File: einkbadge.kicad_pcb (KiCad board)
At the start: 2 copper layers, 108.2 x 99.1 mm, 427 parts, among them J1 USB_C_Receptacle_USB2.0_14P, J2 Conn_01x03, J3 Conn_01x14_Pin, J4 Conn_01x16_Pin, Q1 Si1308EDL, SW1 SW_Push, SW2 SW_Push, SW3 SW_Push, SW4 SW_Push, SW5 SW_Push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

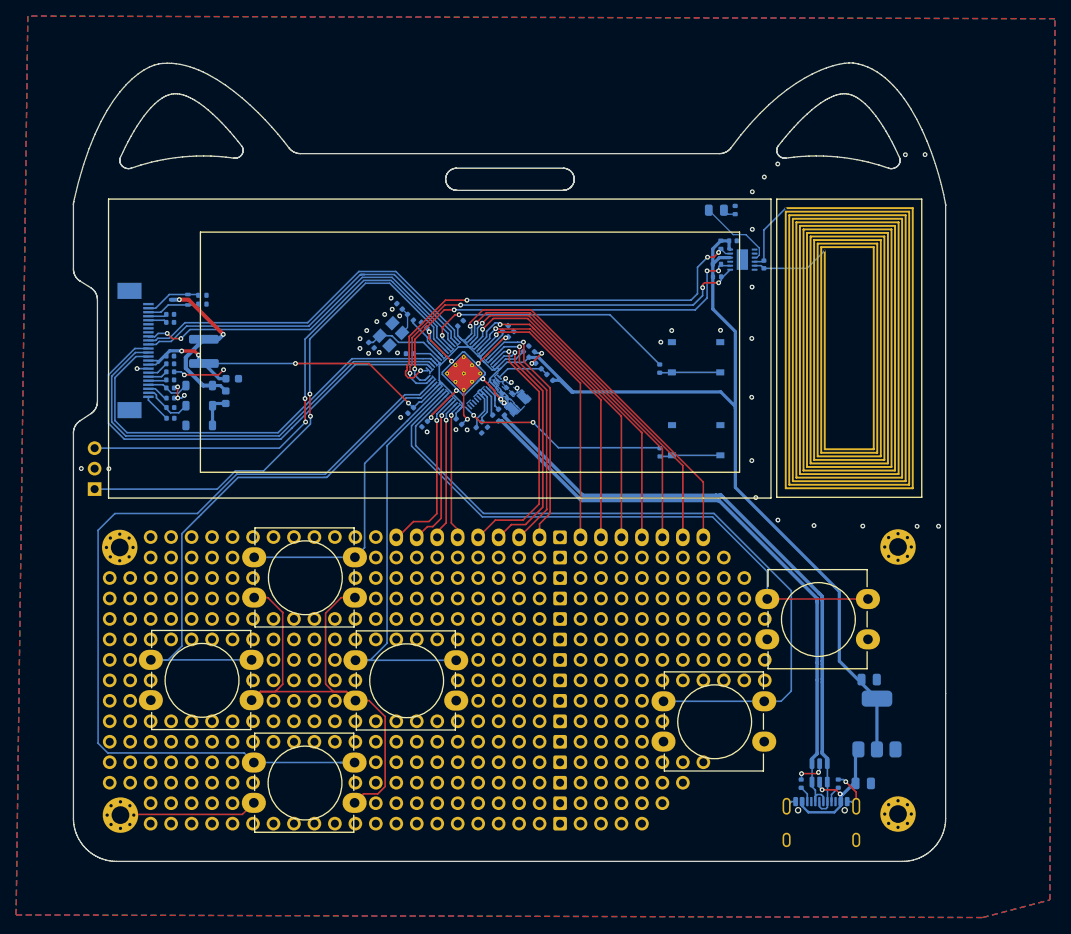
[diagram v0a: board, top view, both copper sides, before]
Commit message: add silkscreen, reroute eink connector
also removed part label silkscreen
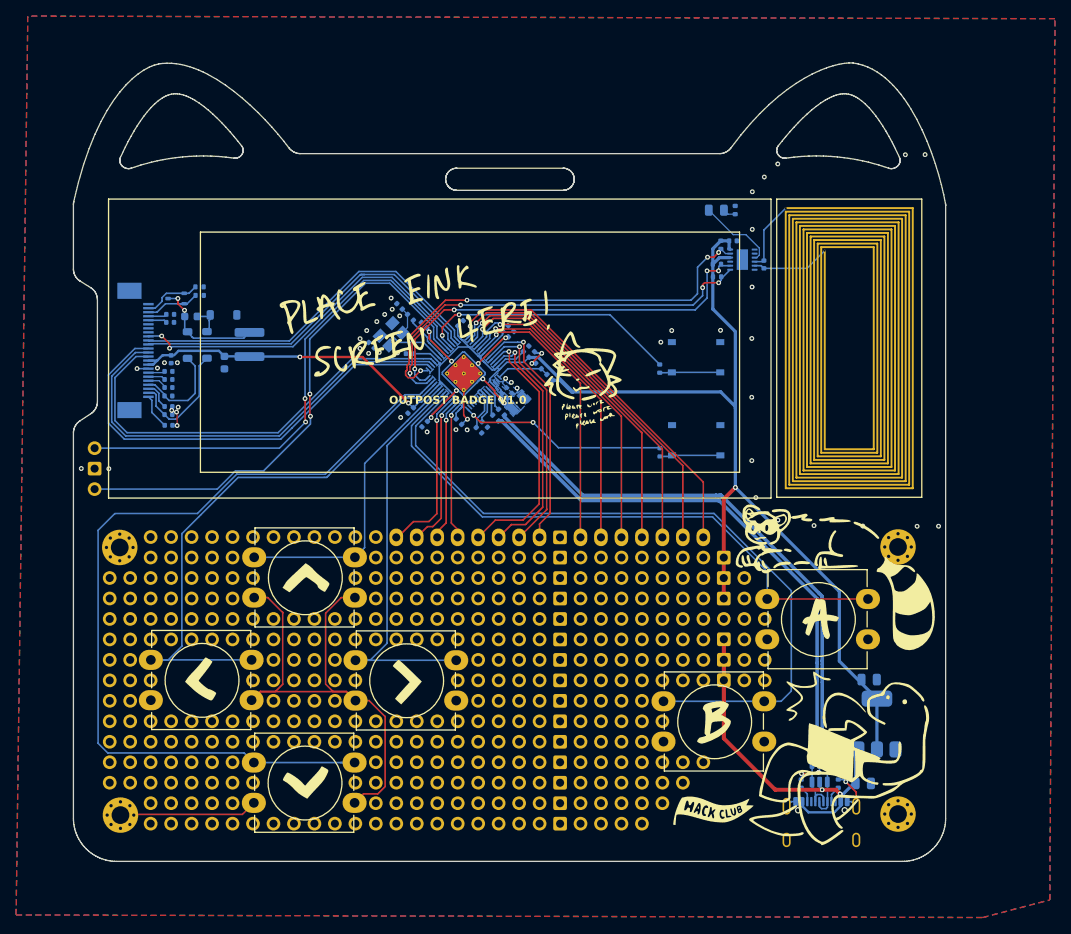
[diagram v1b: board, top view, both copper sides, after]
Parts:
- removed REF**112, REF**152, REF**232, REF**272, REF**312, REF**72: TestPoint_THTPad_D2.0mm_Drill1.0mm, TestPoint:TestPoint_THTPad_D2.0mm_Drill1.0mm
- added G***: LOGO, LOGO, F.Cu at (229.7, 156.9)
- added G***: LOGO, LOGO, F.Cu at (228.3, 114.1)
- added G***: LOGO, LOGO, B.Cu at (201.1, 119.5)
- added J5: Conn_01x03_Pin, Connector_PinHeader_2.54mm:PinHeader_1x03_P2.54mm_Vertical, F.Cu at (231.0, 125.5)
- added J6: Conn_01x03_Pin, Connector_PinHeader_2.54mm:PinHeader_1x03_P2.54mm_Vertical, F.Cu at (231.0, 135.6)
- moved D1 14.0 mm to (168.9, 95.4), turned to 180 degrees
- moved C21 10.9 mm to (164.9, 95.6), turned to 0 degrees
- moved D2 7.60 mm to (166.9, 99.1), turned to -90 degrees
- moved L2 5.72 mm to (172.2, 99.0)
- moved D3 5.23 mm to (164.5, 99.1), turned to 90 degrees
- moved C20 2.22 mm to (169.0, 101.3), turned to -90 degrees
- moved R12 1.14 mm to (166.0, 93.0)
- moved R10 1.10 mm to (165.9, 91.9)
- moved C28 1.07 mm to (162.1, 106.7)
- moved C32 1.02 mm to (162.1, 105.4)
- moved C26 0.97 mm to (162.1, 102.4)
- moved C27 0.97 mm to (162.1, 104.4)
- moved C31 0.97 mm to (162.1, 103.4)
- moved C33 0.91 mm to (162.1, 107.7)
- moved C29 0.91 mm to (162.1, 109.1)
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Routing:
- net +5V: track 20.0 -> 47.1 mm
- net +3V3: track 209.8 -> 226.7 mm, vias 4 -> 3
- net Net-(D3-A): track 26.9 -> 14.4 mm
- net /PREVGL: track 6.21 -> 14.8 mm
- net GND: track 116.2 -> 108.6 mm, vias 51 -> 53
- net /PREVGH: track 5.45 -> 11.8 mm
- net BUSY: track 45.3 -> 46.4 mm
- net RESE: track 6.60 -> 7.60 mm
- net Net-(U5-VCOM): track 4.04 -> 4.82 mm
- net Net-(D1-A): track 4.76 -> 4.00 mm
- net Net-(U5-VSL): track 2.73 -> 3.47 mm
- net Net-(U5-VDD): track 2.69 -> 2.08 mm
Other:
- board text added: "OUTPOST BADGE V1.0"

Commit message: added lcsc part numbers
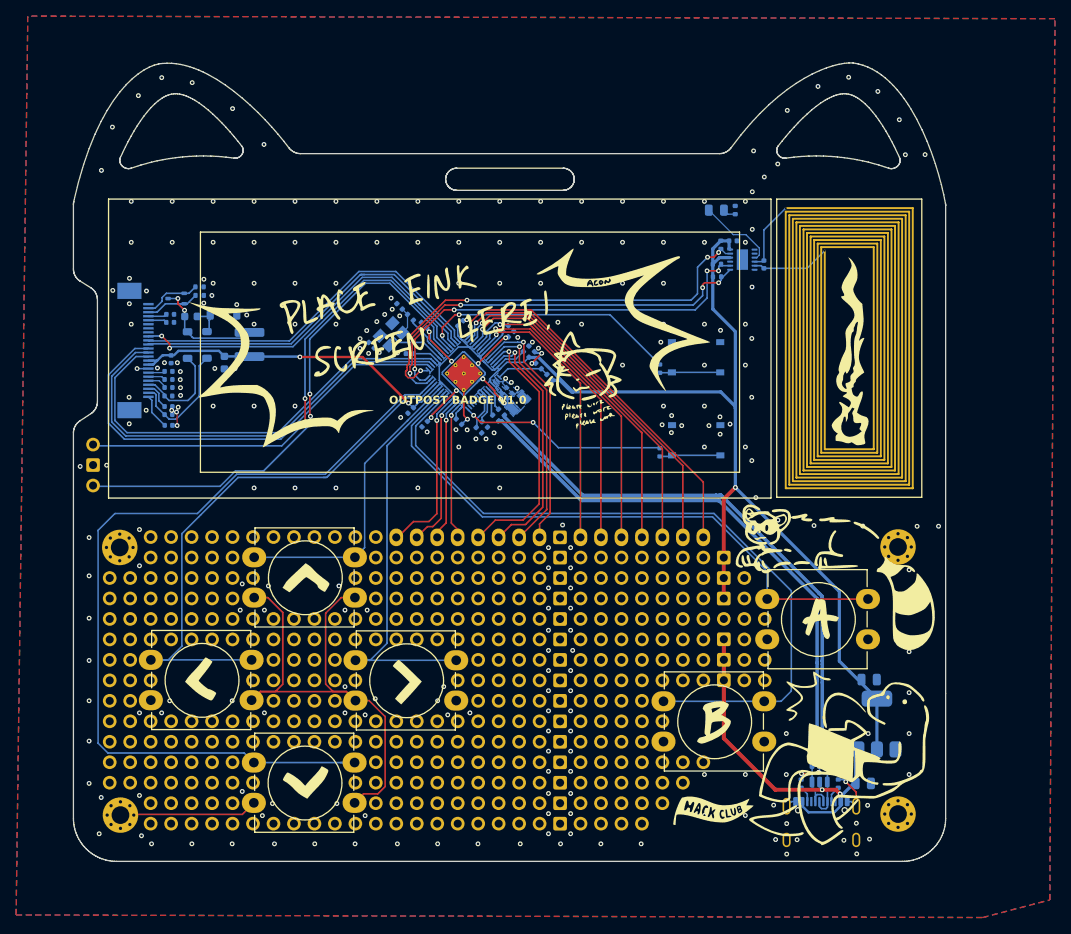
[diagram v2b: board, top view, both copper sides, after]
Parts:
- added G***: LOGO, LOGO, F.Cu at (228.3, 114.1)
- moved J2 0.48 mm to (152.7, 116.5)
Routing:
- net GND: vias 53 -> 274

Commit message: minor routing fix
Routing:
- net GND: track 108.6 -> 109.4 mm, vias 274 -> 275
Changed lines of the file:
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@@
+	)
+	(via
+		(at 234.5 90.36)
+		(size 0.6)
+		(drill 0.3)
+		(layers "F.Cu" "B.Cu")
+		(net 2)
 	)
 	(via
@@
 	)
 	(segment
+		(start 234.8225 89.759999)
+		(end 234.8225 90.0375)
+		(width 0.15)
+		(layer "B.Cu")
+		(net 2)
+	)
+	(segment
 		(start 208.411679 100.131605)
 		(end 207.949083 100.131605)
@@
 		(layer "B.Cu")
 		(net 2)
+	)
+	(segment
+		(start 234.8225 90.0375)
+		(end 234.5 90.36)
+		(width 0.15)
+		(layer "B.Cu")
+		(net 2)
